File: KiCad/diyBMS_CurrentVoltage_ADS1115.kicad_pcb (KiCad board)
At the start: 2 copper layers, 62.2 x 95.6 mm, 51 parts, among them J1 Conn_01x10_MountingPin, J2 Debug/UPDI, J3 Screw_Terminal_01x04, J4 9x9 PIN connector, J5 9x9 PIN connector, J6 Screw_Terminal_01x02, J7 Screw_Terminal_01x02, J8 PA3/PA4, U1 ACPL-C870, U2 ADS1115IDGS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

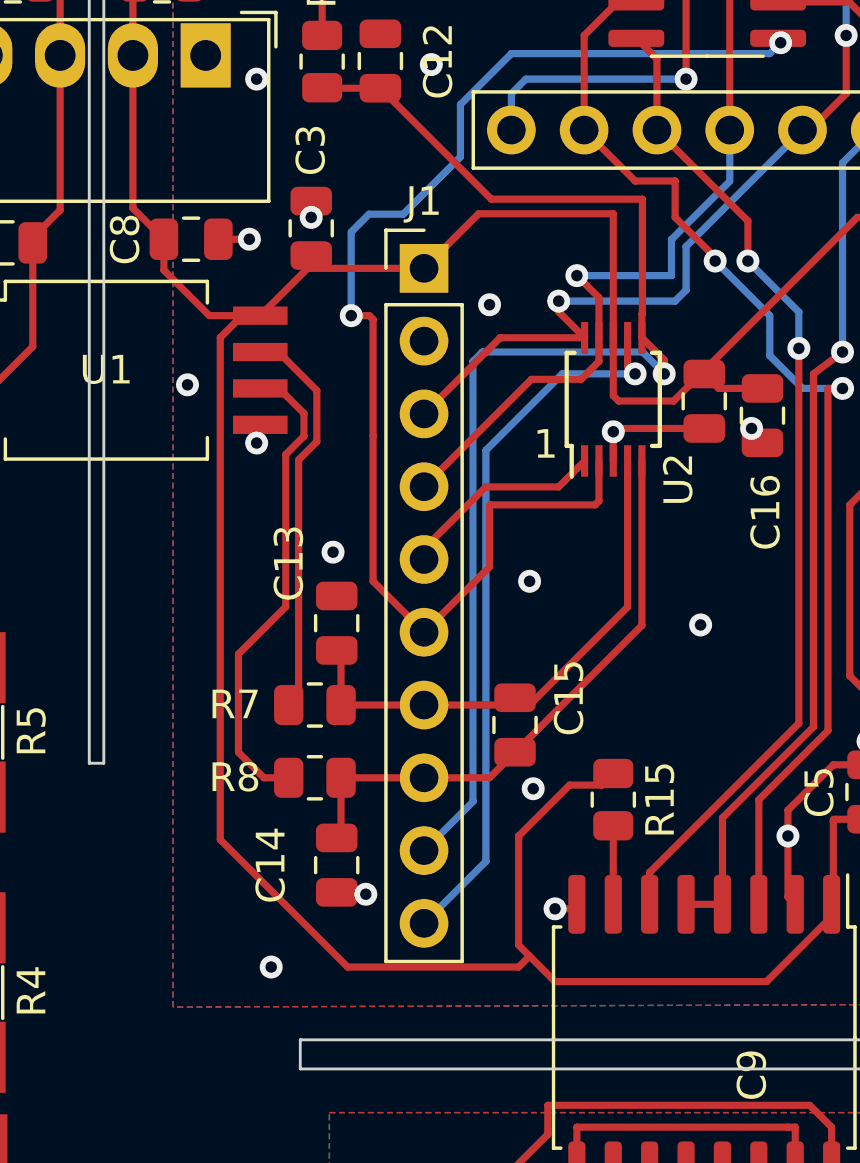
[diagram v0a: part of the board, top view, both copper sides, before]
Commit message: working including MODBUS RTU
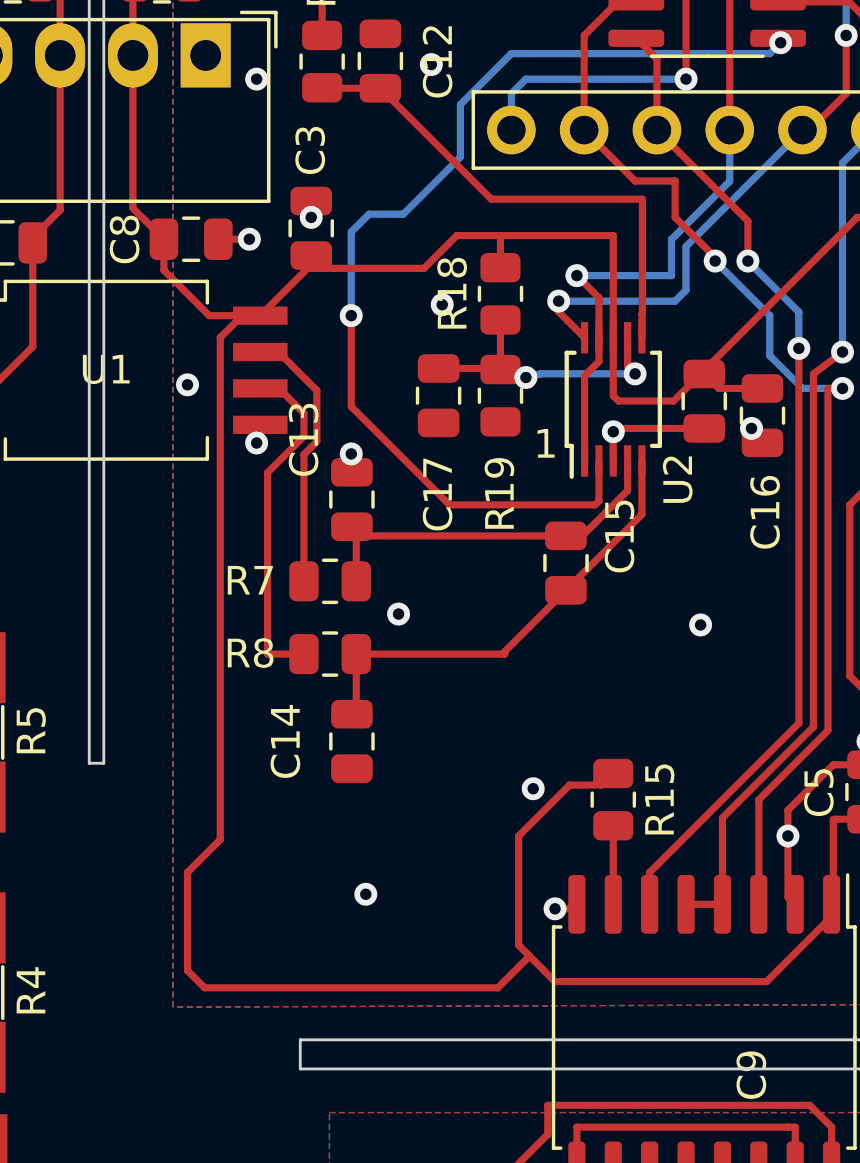
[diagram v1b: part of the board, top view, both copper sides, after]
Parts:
- removed J1: Conn_01x10_MountingPin, Connector_PinHeader_2.54mm:PinHeader_1x10_P2.54mm_Vertical
- added C17: 100n 100V, Capacitor_SMD:C_0805_2012Metric, F.Cu at (56.4, 59.3)
- added R18: 10k, Resistor_SMD:R_0805_2012Metric, F.Cu at (58.5, 55.8)
- added R19: 10k, Resistor_SMD:R_0805_2012Metric, F.Cu at (58.5, 59.3)
- moved C15 5.92 mm to (60.8, 65.2)
- moved R8 4.35 mm to (52.6, 68.3)
- moved C13 4.35 mm to (53.4, 62.9)
- moved C14 4.35 mm to (53.4, 71.4)
- moved R7 4.35 mm to (52.6, 65.8)
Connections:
- U2 pad 1: Net-(J1-Pin_5) -> SDA
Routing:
- net Net-(U2-AIN2): track 44.1 -> 17.6 mm, vias 1 -> 0
- net Net-(U2-AIN3): track 25.1 -> 9.07 mm, vias 1 -> 2
- net ALERT: track 44.9 -> 36.4 mm
- net Net-(J1-Pin_5): track 7.25 -> 0.00 mm
- net SCL: track 35.7 -> 29.0 mm
- net Net-(U2-AIN0): track 18.5 -> 13.4 mm
- net +5V: track 184.5 -> 189.4 mm
- net Net-(U2-AIN1): track 20.6 -> 15.9 mm
- net Net-(U1-OUT-): track 16.8 -> 12.1 mm
- net Net-(U1-OUT+): track 13.9 -> 9.38 mm
- net SDA: track 34.5 -> 30.3 mm
- net GND: vias 24 -> 23
